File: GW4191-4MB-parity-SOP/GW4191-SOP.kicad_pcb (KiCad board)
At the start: 4 copper layers, 88.9 x 20.3 mm, 11 parts, among them J1 DRAM-SIMM-30, U1 4C4M4, U2 4C4M4, U3 4C4M1

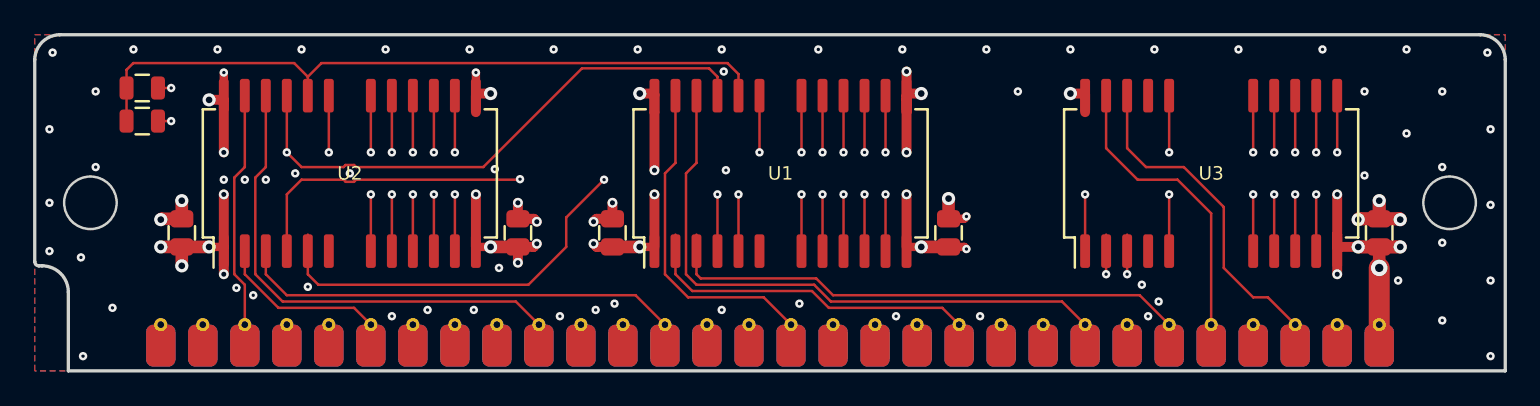
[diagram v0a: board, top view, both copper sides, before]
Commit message: Update to KiCAD 6
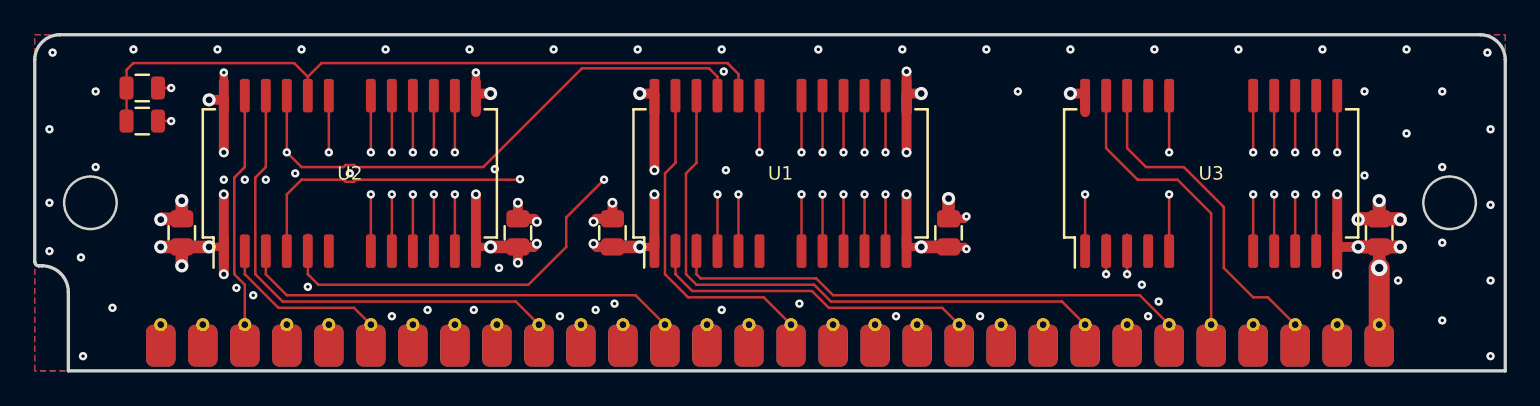
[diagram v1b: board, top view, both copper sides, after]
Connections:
- net /~CASP~ renamed /~{CASP}
- net /~CAS~ renamed /~{CAS}
- net /~OE~ renamed /~{OE}
- net /~RAS~ renamed /~{RAS}
- net /~WE~ renamed /~{WE}
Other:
- net class Default removed
